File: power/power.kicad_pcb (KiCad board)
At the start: 2 copper layers, 66.1 x 64.5 mm, 65 parts, among them J1 Conn_01x02_Female, J10 Conn_01x02_Female, J11 Conn_01x02_Female, J12 Conn_01x02_Female, J13 Conn_01x02_Female, J14 Conn_01x02_Female, J15 Conn_01x03_Male, J2 Barrel_jack, J3 Conn_01x02_Female, J4 Conn_01x02_Female, J5 CONN_02X03, J6 Conn_01x02_Female, J7 Conn_01x02_Female, J8 Conn_01x02_Female, J9 Conn_01x02_Female, Q1 BS170, Q2 BS170, Q3 BS170, Q4 BS170, Q5 BS170, Q6 BS170, U1 ATMEGA16M1, U2 TPS2592xx, U3 LP5907MFX-3_3_NOPB

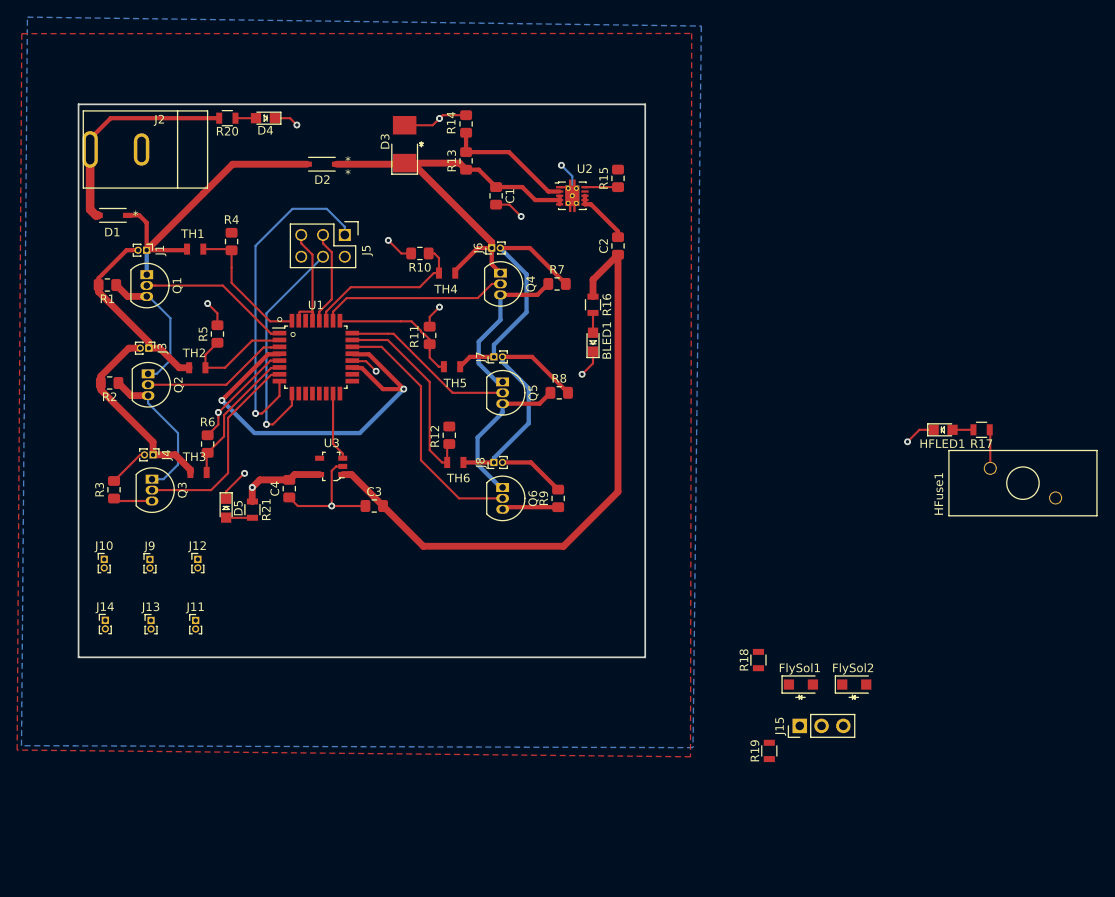
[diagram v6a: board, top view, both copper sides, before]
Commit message: final rev 1: nickel pads added and recovery footprint issues fixed
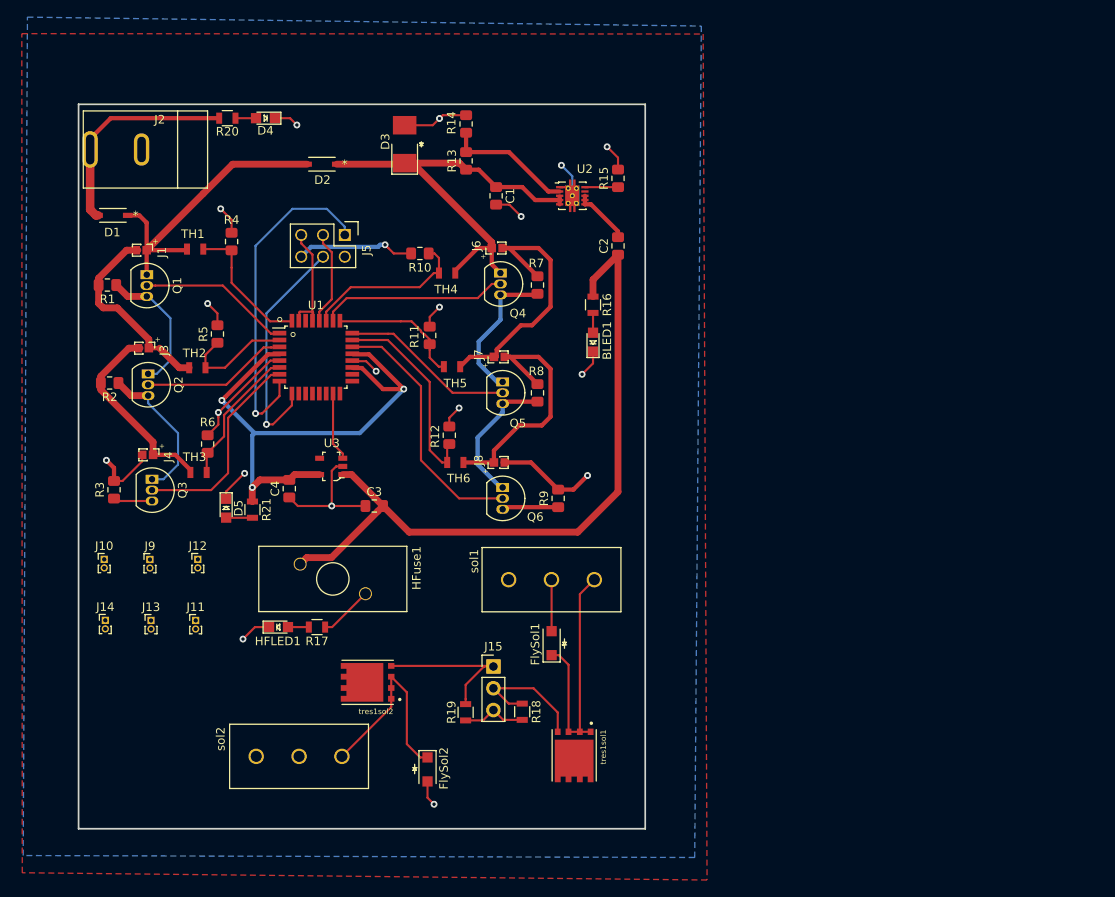
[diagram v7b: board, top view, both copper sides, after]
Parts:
- added sol1: OSTTC03, footprints:OSTTC030162, F.Cu at (186.7, 104.5)
- added sol2: OSTTC03, footprints:OSTTC030162, F.Cu at (157.2, 125.1)
- added tres1sol1: NMOS_CDS16, footprints:TRANS_CSD17312Q5, F.Cu at (189.3, 125.0)
- added tres1sol2: NMOS_CDS16, footprints:TRANS_CSD17312Q5, F.Cu at (165.2, 116.5)
- J1, J3, J4, J6, J7, J8: footprint Connector_PinHeader_1.00mm:PinHeader_1x02_P1.00mm_Vertical -> footprints:nickle_pads_1x2
- moved HFLED1 80.9 mm to (154.8, 110.0)
- moved R17 80.9 mm to (159.3, 110.0)
- moved HFuse1 59.2 mm to (172.3, 104.4), turned to 270 degrees
- moved FlySol2 50.8 mm to (172.2, 126.6), turned to 270 degrees
- moved J15 36.4 mm to (179.9, 114.6), turned to 0 degrees
- moved R19 35.7 mm to (176.7, 119.9), turned to 270 degrees
- moved FlySol1 29.5 mm to (186.7, 111.9), turned to 90 degrees
- moved R18 28.2 mm to (183.3, 119.9), turned to 270 degrees
- moved R8 2.54 mm to (185.0, 82.7), turned to 90 degrees
- moved R7 2.29 mm to (185.0, 70.1), turned to 90 degrees
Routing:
- net GND: track 83.4 -> 127.2 mm, vias 13 -> 19
- net /12V_Solenoid: track 0.00 -> 31.3 mm
- net /12V_Burn_Wire: track 0.00 -> 23.4 mm
- net /burn-wire: track 0.00 -> 18.3 mm
- net /solenoid: track 0.00 -> 15.0 mm
- net +12V: track 72.0 -> 83.1 mm
- net +3V3: track 58.6 -> 65.1 mm
- net Net-(Q5-Pad3): track 18.4 -> 16.5 mm
- net /12V_Switch: track 4.52 -> 6.32 mm
- net Net-(Q4-Pad3): track 18.8 -> 17.1 mm
- net /B1B-: track 29.3 -> 31.0 mm
- net /B2B-: track 28.2 -> 29.8 mm
- net /B1A-: track 21.6 -> 23.1 mm
- net /B2A-: track 22.5 -> 23.0 mm
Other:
- board size 66.1 x 64.5 mm -> 66.1 x 84.5 mm

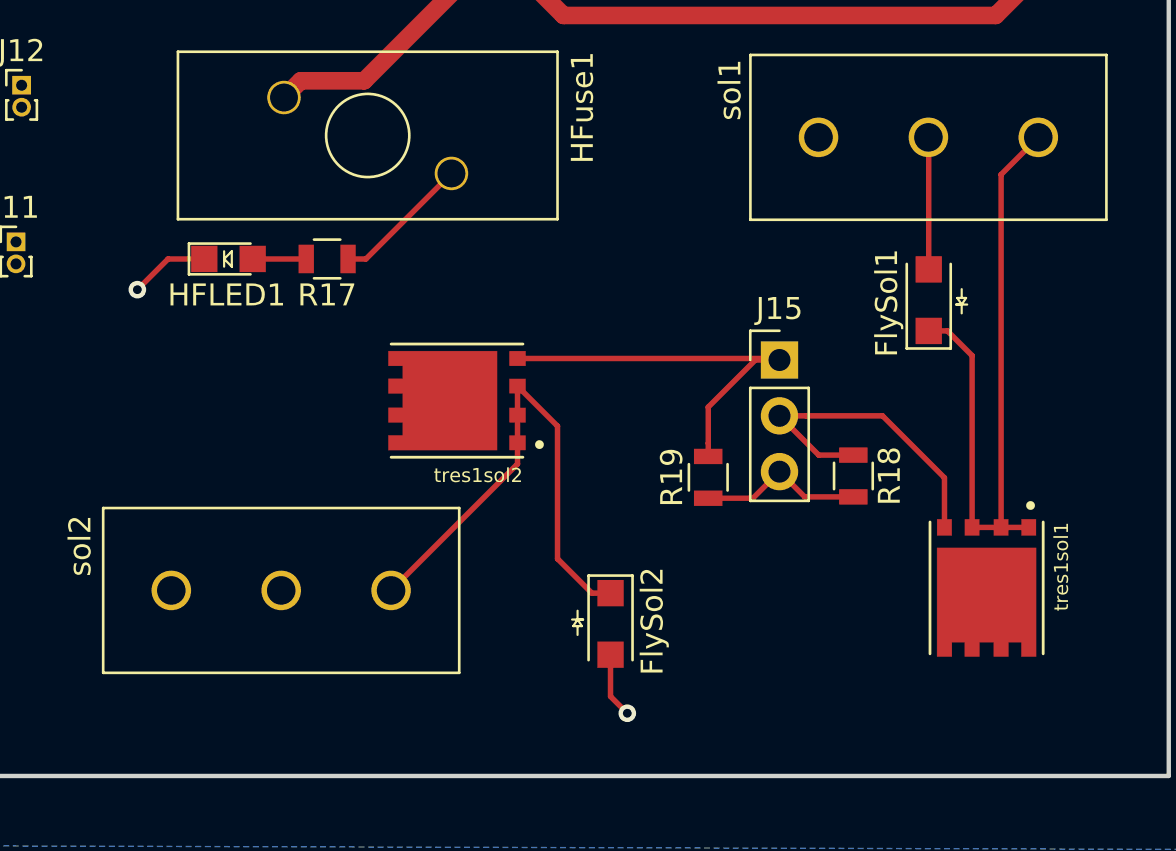
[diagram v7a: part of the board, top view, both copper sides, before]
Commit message: ribbon added to sch and recovery wires increased and no connects added
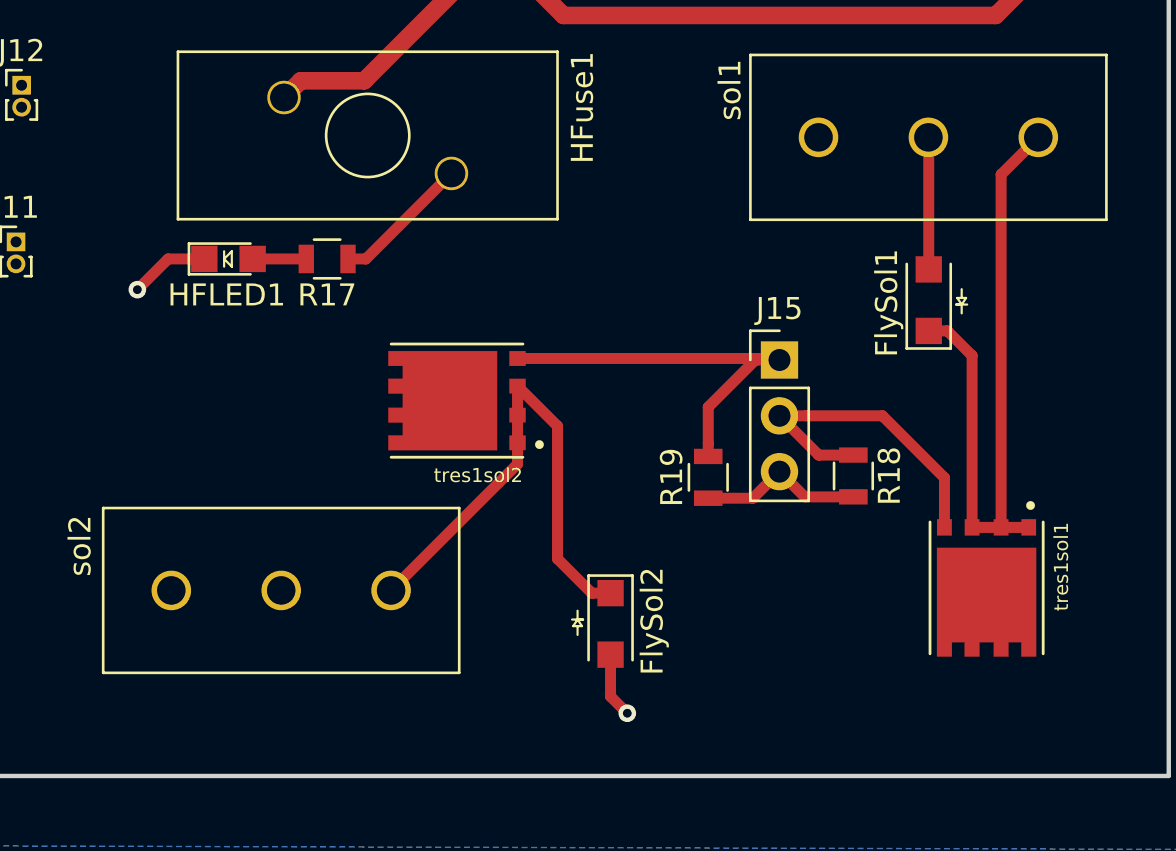
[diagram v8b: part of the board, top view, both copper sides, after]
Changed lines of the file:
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@@
   )
   (setup
-    (last_trace_width 0.5)
+    (last_trace_width 0.25)
     (user_trace_width 0.5)
     (user_trace_width 0.8)
@@
   (segment (start 154.401966 50.638542) (end 156.175542 50.638542) (width 0.25) (layer F.Cu) (net 2))
   (segment (start 156.175542 50.638542) (end 156.972 51.435) (width 0.25) (layer F.Cu) (net 2))
-  (via (at 150.680862 111.409539) (size 0.8) (drill 0.4) (layers F.Cu B.Cu) (net 2))
-  (segment (start 153.728862 110.012539) (end 152.077862 110.012539) (width 0.25) (layer F.Cu) (net 2))
-  (segment (start 152.077862 110.012539) (end 150.680862 111.409539) (width 0.25) (layer F.Cu) (net 2))
+  (via (at 150.680862 111.409539) (size 0.8) (drill 0.4) (layers F.Cu B.Cu) (net 2) (status 1000000))
+  (segment (start 152.077862 110.012539) (end 150.680862 111.409539) (width 0.5) (layer F.Cu) (net 2) (status 1000000))
+  (segment (start 153.728862 110.012539) (end 152.077862 110.012539) (width 0.5) (layer F.Cu) (net 2) (status 1000000))
   (via (at 190.246 80.518) (size 0.8) (drill 0.4) (layers F.Cu B.Cu) (net 2))
   (segment (start 191.521076 77.867738) (end 191.521076 79.242924) (width 0.25) (layer F.Cu) (net 2))
   (segment (start 191.521076 79.242924) (end 190.246 80.518) (width 0.25) (layer F.Cu) (net 2))
-  (segment (start 178.690783 120.899) (end 179.899509 119.690274) (width 0.25) (layer F.Cu) (net 2))
-  (segment (start 176.657 120.899) (end 178.690783 120.899) (width 0.25) (layer F.Cu) (net 2))
-  (segment (start 181.047235 120.838) (end 179.899509 119.690274) (width 0.25) (layer F.Cu) (net 2))
-  (segment (start 183.261 120.838) (end 181.047235 120.838) (width 0.25) (layer F.Cu) (net 2))
-  (segment (start 186.69 104.493965) (end 186.675252 104.479217) (width 0.25) (layer F.Cu) (net 2))
-  (segment (start 186.69 110.487) (end 186.69 104.493965) (width 0.25) (layer F.Cu) (net 2))
+  (segment (start 178.690783 120.899) (end 179.899509 119.690274) (width 0.5) (layer F.Cu) (net 2))
+  (segment (start 176.657 120.899) (end 178.690783 120.899) (width 0.5) (layer F.Cu) (net 2))
+  (segment (start 181.047235 120.838) (end 179.899509 119.690274) (width 0.5) (layer F.Cu) (net 2))
+  (segment (start 183.261 120.838) (end 181.047235 120.838) (width 0.5) (layer F.Cu) (net 2))
+  (segment (start 186.69 104.493965) (end 186.675252 104.479217) (width 0.5) (layer F.Cu) (net 2))
+  (segment (start 186.69 110.487) (end 186.69 104.493965) (width 0.5) (layer F.Cu) (net 2))
   (via (at 172.974 130.683) (size 0.8) (drill 0.4) (layers F.Cu B.Cu) (net 2))
-  (segment (start 172.212 128.019) (end 172.212 129.921) (width 0.25) (layer F.Cu) (net 2))
-  (segment (start 172.212 129.921) (end 172.974 130.683) (width 0.25) (layer F.Cu) (net 2))
+  (segment (start 172.212 129.921) (end 172.974 130.683) (width 0.5) (layer F.Cu) (net 2))
+  (segment (start 172.212 128.019) (end 172.212 129.921) (width 0.5) (layer F.Cu) (net 2))
   (via (at 175.895 84.455) (size 0.8) (drill 0.4) (layers F.Cu B.Cu) (net 2))
   (segment (start 174.752 86.605) (end 174.752 85.598) (width 0.25) (layer F.Cu) (net 2))
@@
   (segment (start 148.737362 97.259362) (end 148.717 97.239) (width 0.25) (layer F.Cu) (net 37))
   (segment (start 151.78653 97.259362) (end 148.737362 97.259362) (width 0.25) (layer F.Cu) (net 37))
-  (segment (start 191.240578 122.227354) (end 189.983078 122.227354) (width 0.25) (layer F.Cu) (net 38))
-  (segment (start 189.983078 122.227354) (end 188.663078 122.227354) (width 0.25) (layer F.Cu) (net 38))
-  (segment (start 188.663078 114.410078) (end 187.54 113.287) (width 0.25) (layer F.Cu) (net 38))
-  (segment (start 187.54 113.287) (end 186.69 113.287) (width 0.25) (layer F.Cu) (net 38))
-  (segment (start 188.663078 122.227354) (end 188.663078 114.410078) (width 0.25) (layer F.Cu) (net 38))
-  (segment (start 189.983078 106.171391) (end 191.675252 104.479217) (width 0.25) (layer F.Cu) (net 38))
-  (segment (start 189.983078 122.227354) (end 189.983078 106.171391) (width 0.25) (layer F.Cu) (net 38))
-  (segment (start 167.9795 115.799) (end 167.9795 117.119) (width 0.25) (layer F.Cu) (net 39))
-  (segment (start 167.9795 117.119) (end 167.9795 118.3765) (width 0.25) (layer F.Cu) (net 39))
-  (segment (start 167.9795 119.3415) (end 162.226 125.095) (width 0.25) (layer F.Cu) (net 39))
-  (segment (start 167.9795 118.3765) (end 167.9795 119.3415) (width 0.25) (layer F.Cu) (net 39))
-  (segment (start 171.362 125.219) (end 172.212 125.219) (width 0.25) (layer F.Cu) (net 39))
-  (segment (start 169.799 123.656) (end 171.362 125.219) (width 0.25) (layer F.Cu) (net 39))
-  (segment (start 167.9795 115.799) (end 169.799 117.6185) (width 0.25) (layer F.Cu) (net 39))
-  (segment (start 169.799 117.6185) (end 169.799 123.656) (width 0.25) (layer F.Cu) (net 39))
-  (segment (start 158.366862 110.012539) (end 155.928862 110.012539) (width 0.25) (layer F.Cu) (net 40))
-  (segment (start 161.081661 110.012539) (end 164.973 106.1212) (width 0.25) (layer F.Cu) (net 41))
-  (segment (start 160.266862 110.012539) (end 161.081661 110.012539) (width 0.25) (layer F.Cu) (net 41))
-  (segment (start 181.687235 118.938) (end 179.899509 117.150274) (width 0.25) (layer F.Cu) (net 42))
-  (segment (start 183.261 118.938) (end 181.687235 118.938) (width 0.25) (layer F.Cu) (net 42))
-  (segment (start 181.10159 117.150274) (end 179.899509 117.150274) (width 0.25) (layer F.Cu) (net 42))
-  (segment (start 184.587274 117.150274) (end 181.10159 117.150274) (width 0.25) (layer F.Cu) (net 42))
-  (segment (start 187.405578 122.227354) (end 187.405578 119.968578) (width 0.25) (layer F.Cu) (net 42))
-  (segment (start 187.405578 119.968578) (end 184.587274 117.150274) (width 0.25) (layer F.Cu) (net 42))
-  (segment (start 176.657 116.752783) (end 176.657 118.399) (width 0.25) (layer F.Cu) (net 43))
-  (segment (start 178.799509 114.610274) (end 176.657 116.752783) (width 0.25) (layer F.Cu) (net 43))
-  (segment (start 179.899509 114.610274) (end 178.799509 114.610274) (width 0.25) (layer F.Cu) (net 43))
-  (segment (start 176.657 118.399) (end 176.657 118.999) (width 0.25) (layer F.Cu) (net 43))
-  (segment (start 179.830735 114.5415) (end 179.899509 114.610274) (width 0.25) (layer F.Cu) (net 43))
-  (segment (start 167.9795 114.5415) (end 179.830735 114.5415) (width 0.25) (layer F.Cu) (net 43))
+  (segment (start 191.240578 122.227354) (end 189.983078 122.227354) (width 0.5) (layer F.Cu) (net 38))
+  (segment (start 189.983078 122.227354) (end 188.663078 122.227354) (width 0.5) (layer F.Cu) (net 38))
+  (segment (start 188.663078 114.410078) (end 187.54 113.287) (width 0.5) (layer F.Cu) (net 38))
+  (segment (start 188.663078 122.227354) (end 188.663078 114.410078) (width 0.5) (layer F.Cu) (net 38))
+  (segment (start 187.54 113.287) (end 186.69 113.287) (width 0.5) (layer F.Cu) (net 38))
+  (segment (start 189.983078 106.171391) (end 191.675252 104.479217) (width 0.5) (layer F.Cu) (net 38))
+  (segment (start 189.983078 122.227354) (end 189.983078 106.171391) (width 0.5) (layer F.Cu) (net 38))
+  (segment (start 167.9795 115.799) (end 167.9795 117.119) (width 0.5) (layer F.Cu) (net 39))
+  (segment (start 167.9795 117.119) (end 167.9795 118.3765) (width 0.5) (layer F.Cu) (net 39))
+  (segment (start 167.9795 119.3415) (end 162.226 125.095) (width 0.5) (layer F.Cu) (net 39))
+  (segment (start 167.9795 118.3765) (end 167.9795 119.3415) (width 0.5) (layer F.Cu) (net 39))
+  (segment (start 171.362 125.219) (end 172.212 125.219) (width 0.5) (layer F.Cu) (net 39))
+  (segment (start 169.799 117.6185) (end 169.799 123.656) (width 0.5) (layer F.Cu) (net 39))
+  (segment (start 167.9795 115.799) (end 169.799 117.6185) (width 0.5) (layer F.Cu) (net 39))
+  (segment (start 169.799 123.656) (end 171.362 125.219) (width 0.5) (layer F.Cu) (net 39))
+  (segment (start 158.366862 110.012539) (end 155.928862 110.012539) (width 0.5) (layer F.Cu) (net 40))
+  (segment (start 161.081661 110.012539) (end 164.973 106.1212) (width 0.5) (layer F.Cu) (net 41))
+  (segment (start 160.266862 110.012539) (end 161.081661 110.012539) (width 0.5) (layer F.Cu) (net 41))
+  (segment (start 181.687235 118.938) (end 179.899509 117.150274) (width 0.5) (layer F.Cu) (net 42))
+  (segment (start 183.261 118.938) (end 181.687235 118.938) (width 0.5) (layer F.Cu) (net 42))
+  (segment (start 181.10159 117.150274) (end 179.899509 117.150274) (width 0.5) (layer F.Cu) (net 42))
+  (segment (start 187.405578 119.968578) (end 184.587274 117.150274) (width 0.5) (layer F.Cu) (net 42))
+  (segment (start 187.405578 122.227354) (end 187.405578 119.968578) (width 0.5) (layer F.Cu) (net 42))
+  (segment (start 184.587274 117.150274) (end 181.10159 117.150274) (width 0.5) (layer F.Cu) (net 42))
+  (segment (start 176.657 116.752783) (end 176.657 118.399) (width 0.5) (layer F.Cu) (net 43))
+  (segment (start 176.657 118.399) (end 176.657 118.999) (width 0.5) (layer F.Cu) (net 43))
+  (segment (start 179.899509 114.610274) (end 178.799509 114.610274) (width 0.5) (layer F.Cu) (net 43))
+  (segment (start 178.799509 114.610274) (end 176.657 116.752783) (width 0.5) (layer F.Cu) (net 43))
+  (segment (start 179.830735 114.5415) (end 179.899509 114.610274) (width 0.5) (layer F.Cu) (net 43))
+  (segment (start 167.9795 114.5415) (end 179.830735 114.5415) (width 0.5) (layer F.Cu) (net 43))
   (segment (start 180.34 81.407) (end 180.975 81.407) (width 0.5) (layer B.Cu) (net 44))
   (segment (start 178.181 79.248) (end 180.34 81.407) (width 0.5) (layer B.Cu) (net 44))
